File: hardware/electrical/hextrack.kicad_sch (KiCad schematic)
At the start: 0 parts

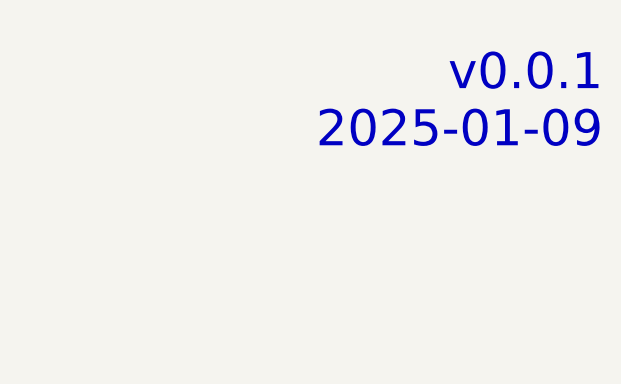
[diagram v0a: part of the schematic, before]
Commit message: Update schematic to include regulators and switches, update render
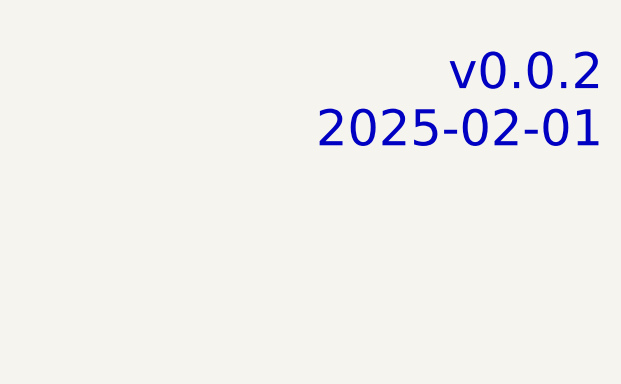
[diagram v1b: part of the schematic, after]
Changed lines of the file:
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@@
 	(title_block
 		(title "HexTrack PCB")
-		(date "2025-01-09")
-		(rev "v0.0.1")
+		(date "2025-02-01")
+		(rev "v0.0.2")
 		(company "TMShader")
 		(comment 9 "HexTrack")
